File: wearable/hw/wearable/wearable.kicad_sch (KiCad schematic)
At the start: 39 parts, among them Q20 ${ALTIUM_VALUE}, Q21 ${ALTIUM_VALUE}, U2 ${ALTIUM_VALUE}, X20 ${ALTIUM_VALUE}

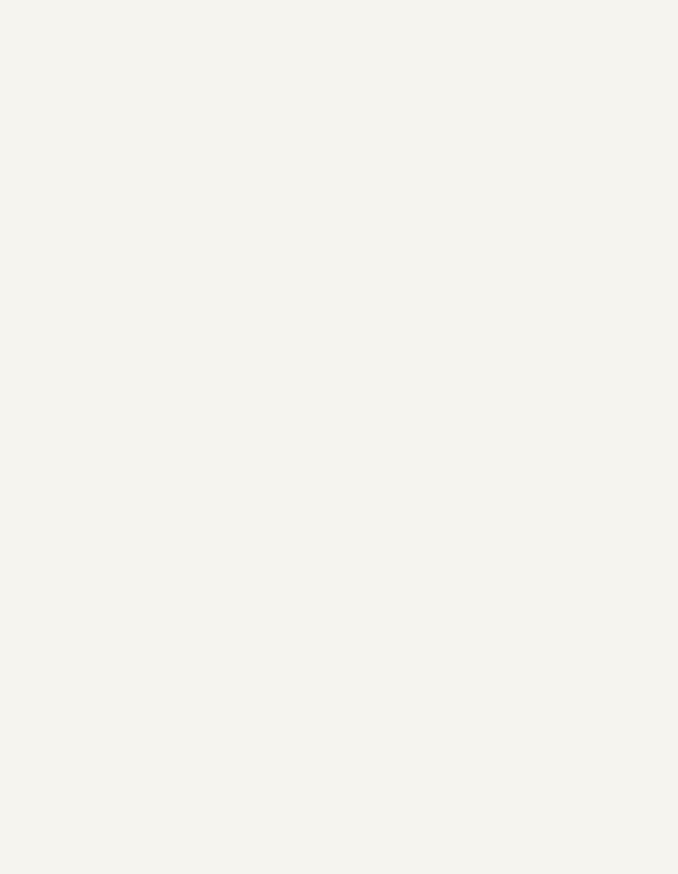
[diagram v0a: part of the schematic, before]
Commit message: Added symbols and stuff to library
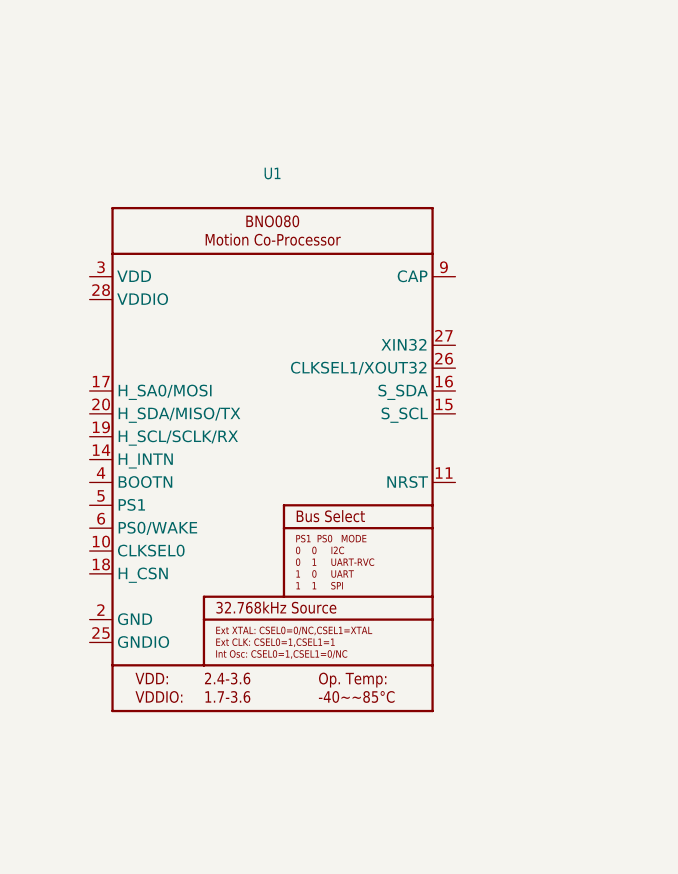
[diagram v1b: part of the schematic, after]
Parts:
- added U1: ~, Adafruit_BNO08x:BNO080, symbol BNO085:BNO080

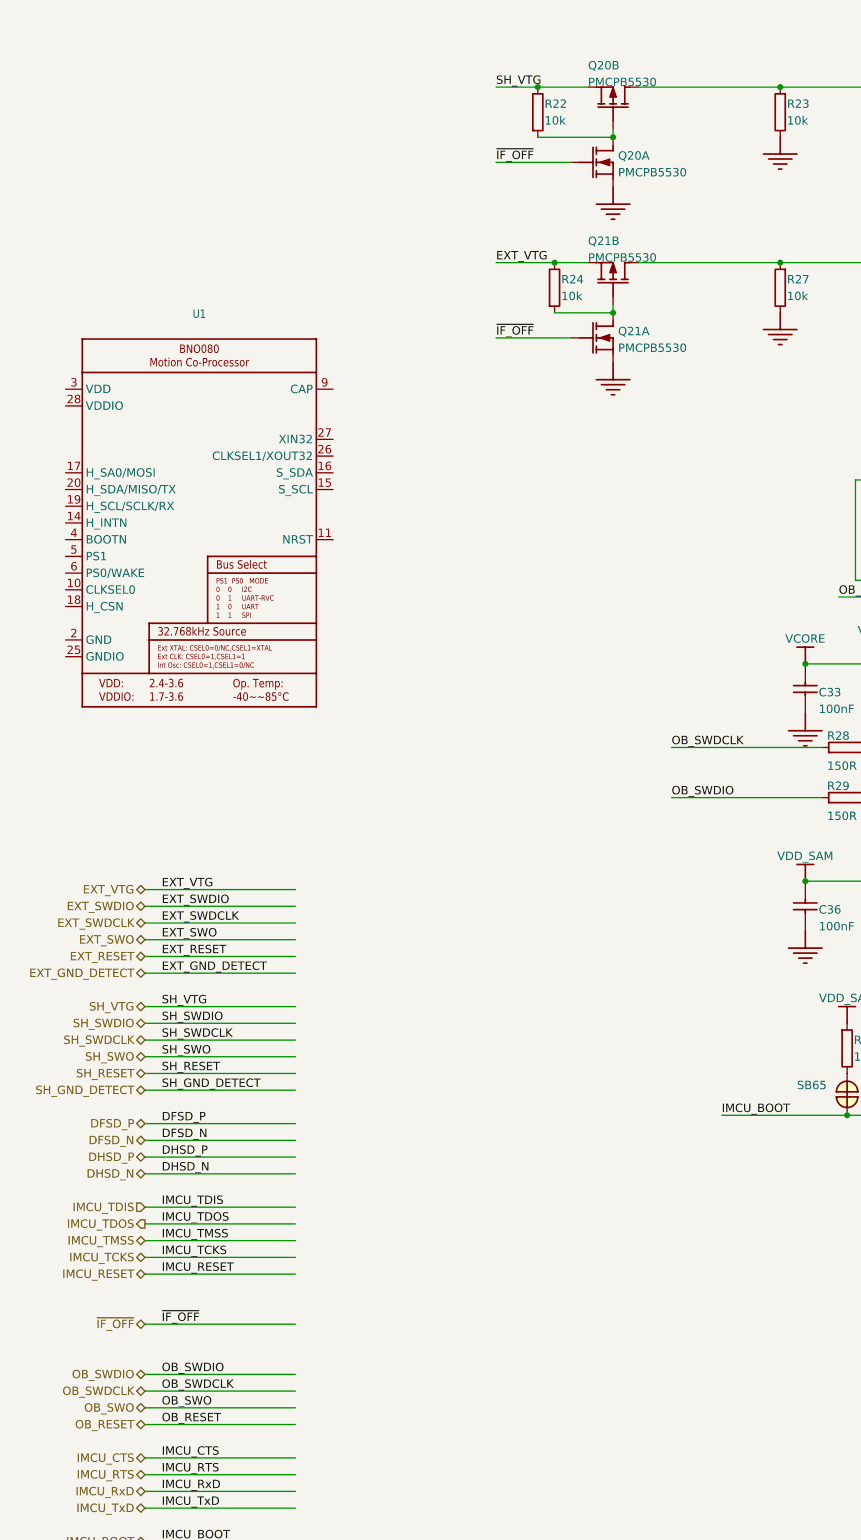
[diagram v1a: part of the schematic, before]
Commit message: Updated schematic with needed parts
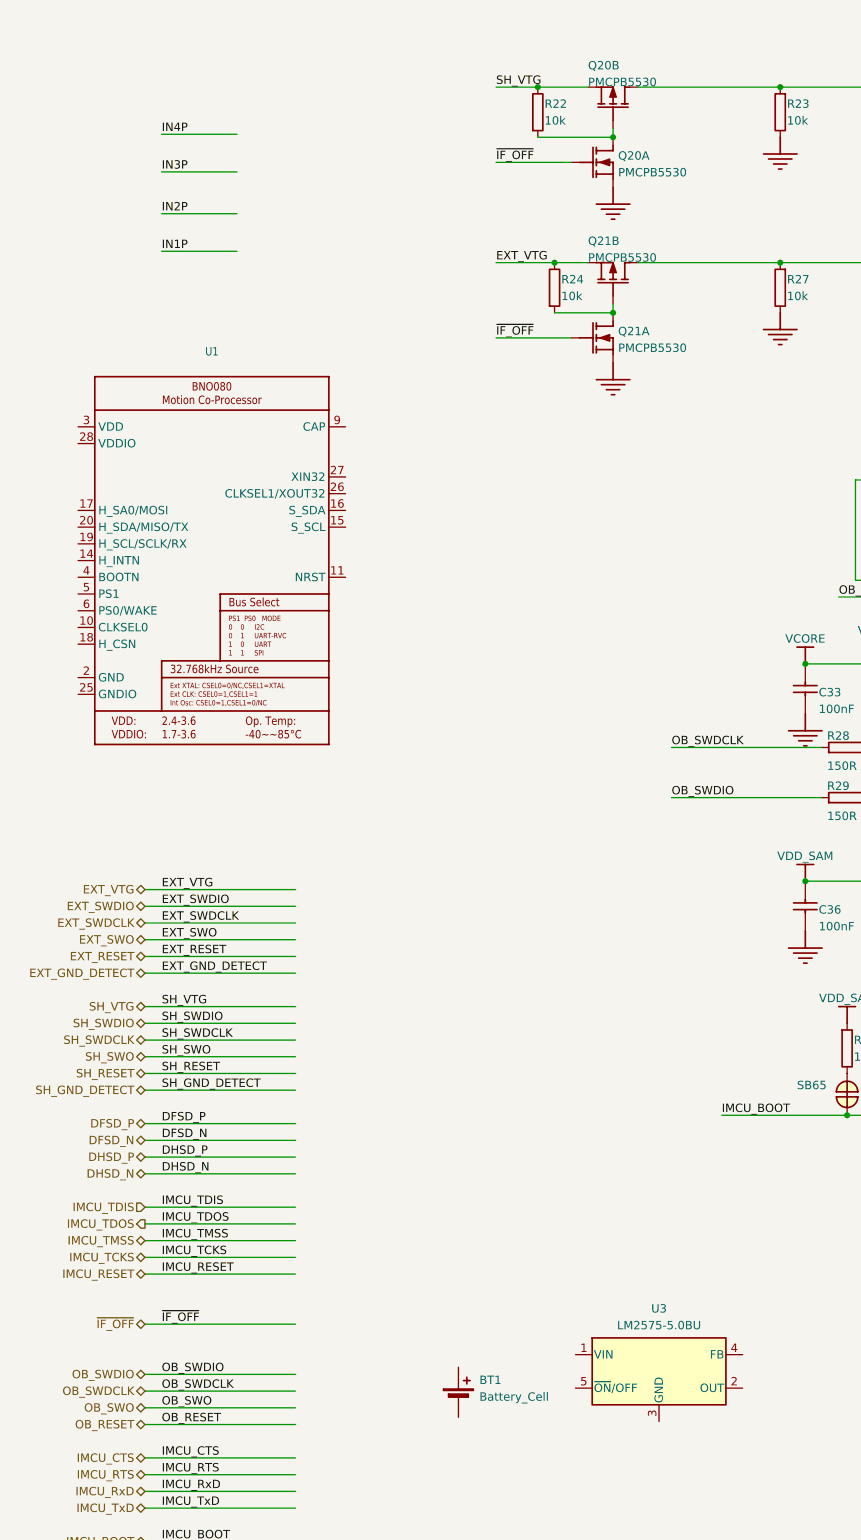
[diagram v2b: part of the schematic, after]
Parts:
- added BT1: Battery_Cell, symbol Device:Battery_Cell
- added U3: LM2575-5.0BU, Package_TO_SOT_SMD:TO-263-5_TabPin3, symbol Regulator_Switching:LM2575-5.0BU
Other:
- moved on the sheet: U1

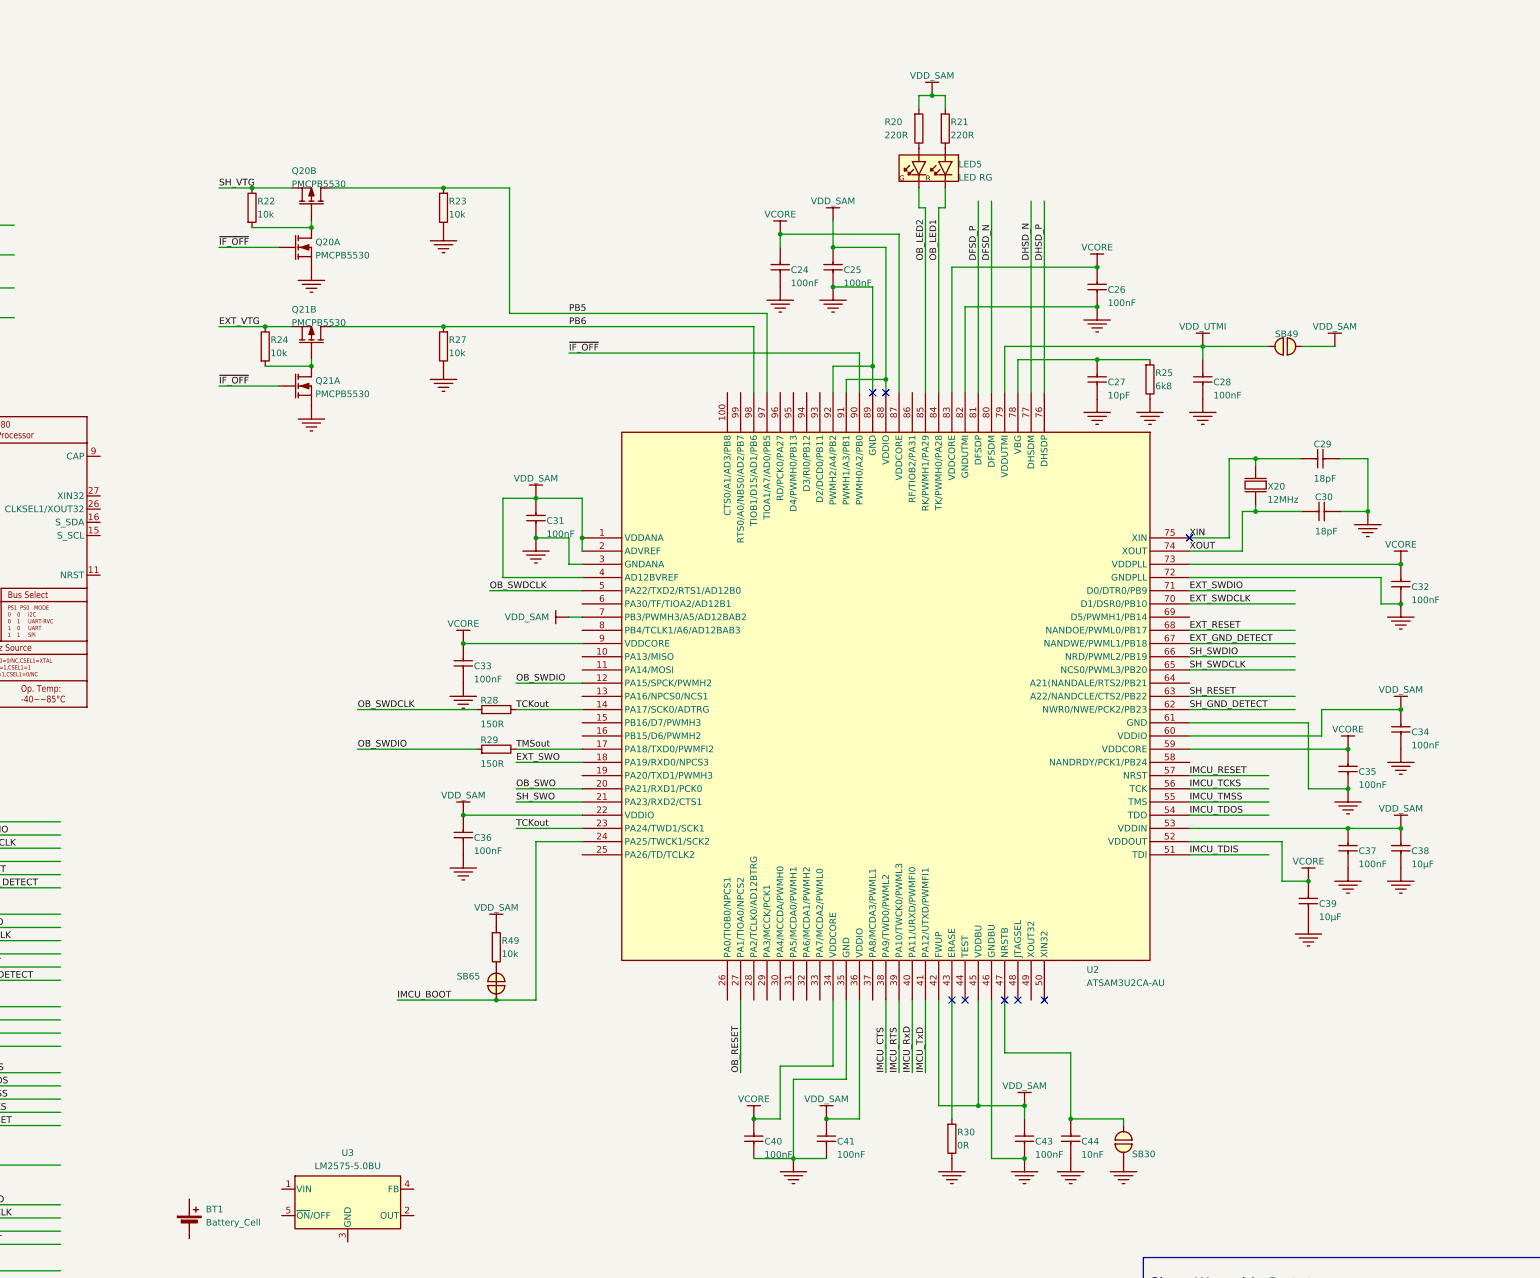
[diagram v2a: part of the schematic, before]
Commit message: Added 445L footprints/symbols and changed some stuff
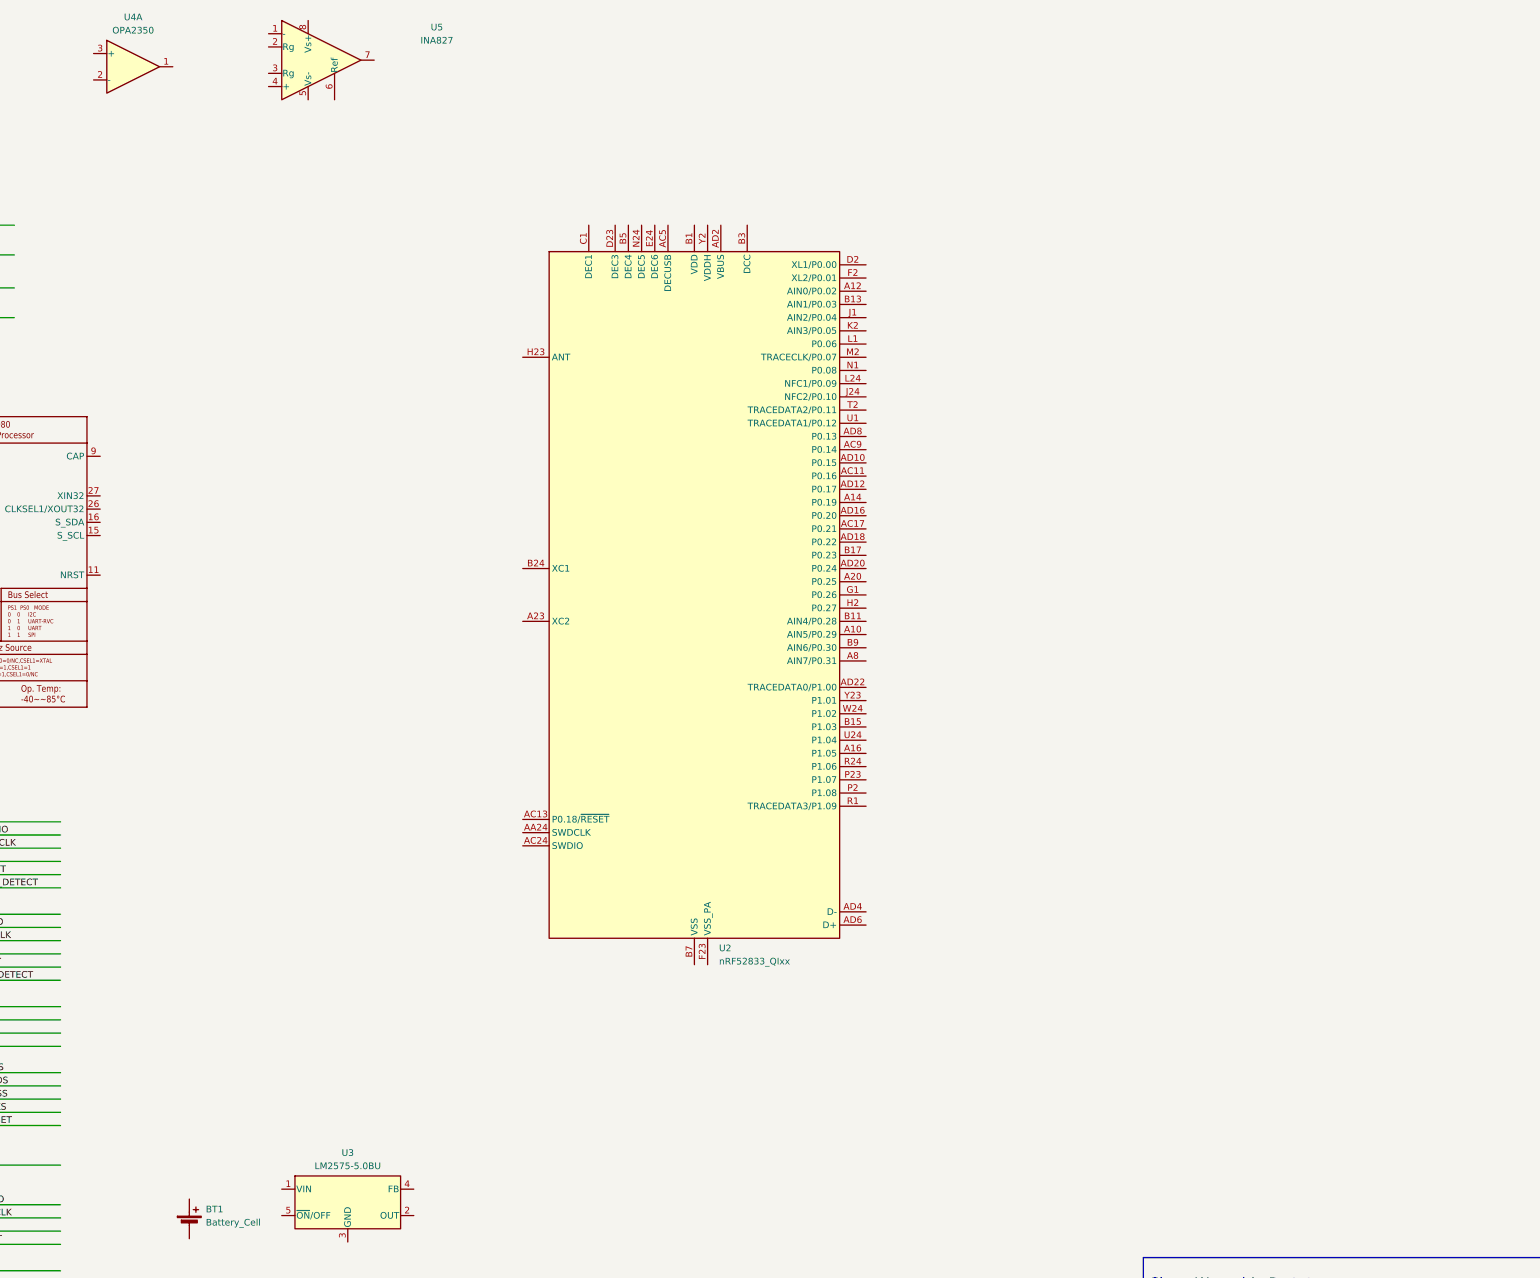
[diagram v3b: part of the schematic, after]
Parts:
- removed C24, C25, C26, C27, C28, C31, C33, C34, C35, C36, C37, C40, C41, C43, C44: ${ALTIUM_VALUE}, CAPC0603X03L_C, symbol wearable-altium-import:root_1_CAP
- removed C29, C30: ${ALTIUM_VALUE}, CAPC0603X03L_C, symbol wearable-altium-import:root_0_CAP
- removed C32: ${ALTIUM_VALUE}, CAPC0603X03L_C, symbol wearable-altium-import:root_3_CAP
- removed C38, C39: ${ALTIUM_VALUE}, CAPC1608X06L, symbol wearable-altium-import:root_1_CAP
- removed LED5: ${ALTIUM_VALUE}, LED_DUAL_0606, symbol wearable-altium-import:root_0_mirrored_D{colon}LED_DUAL_RG
- removed Q20: ${ALTIUM_VALUE}, PMCPB5530X, symbol wearable-altium-import:root_1_T{colon}FET-N/P-DUAL
- removed Q21: ${ALTIUM_VALUE}, PMCPB5530X, symbol wearable-altium-import:root_0_T{colon}FET-N/P-DUAL
- removed R20, R21, R25, R30, R49: ${ALTIUM_VALUE}, RESC0603X03L_C, symbol wearable-altium-import:root_1_RES
- removed R22, R24: ${ALTIUM_VALUE}, RESC0603X03L_C, symbol wearable-altium-import:root_3_mirrored_RES
- removed R23, R27: ${ALTIUM_VALUE}, RESC0603X03L_C, symbol wearable-altium-import:root_1_mirrored_RES
- removed R28, R29: ${ALTIUM_VALUE}, RESC0603X03L_C, symbol wearable-altium-import:root_2_RES
- removed SB30: ${ALTIUM_VALUE}, Solderbridge, symbol wearable-altium-import:root_1_SOLDERBRIDGE
- removed SB49: ${ALTIUM_VALUE}, Solderbridge, symbol wearable-altium-import:root_0_SOLDERBRIDGE
- removed SB65: ${ALTIUM_VALUE}, Solderbridge_Shorted, symbol wearable-altium-import:root_3_SOLDERBRIDGE_SHORTED
- removed U2: ${ALTIUM_VALUE}, TSQFP50P1600X1600X160-100N, symbol wearable-altium-import:root_0_ATSAM3UxCA-AU
- removed X20: ${ALTIUM_VALUE}, BT-XTAL_3225, symbol wearable-altium-import:root_1_XTAL_4-pin_grounded
- added U2: nRF52833_QIxx, Package_DFN_QFN:Nordic_AQFN-73-1EP_7x7mm_P0.5mm, symbol MCU_Nordic:nRF52833_QIxx
- added U4: OPA2350, ECE445L:DIP-8_W7.62mm_LongPads, symbol ECE 445L_old:OPA2350
- added U5: INA827, ECE445L:VSSOP-8_3.0x3.0mm_P0.65mm, symbol ECE 445L_old:INA827
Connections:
- new net: U2.A22 (VDD), U2.AD14 (VDD), U2.AD23 (VDD), U2.B1 (VDD), U2.W1 (VDD)
- new net: U2.B7 (VSS), U2.EP (VSS)
- no-connect marks 8 -> 0

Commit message: hw
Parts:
- removed U4: OPA2350, ECE445L:DIP-8_W7.62mm_LongPads, symbol ECE 445L_old:OPA2350
- removed U5: INA827, ECE445L:VSSOP-8_3.0x3.0mm_P0.65mm, symbol ECE 445L_old:INA827
- added C1, C2: 2uF, symbol Device:C
- added C3, C5: 0.1uF, symbol Device:C
- added C4: 3.3uF, symbol Device:C
- added C6, C7, C8: 0.015uF, symbol Device:C
- added D1: MBR360, DIOAD2860W130L840D505, symbol MBR360:MBR360
- added IC1: AD627ANZ, DIP794W56P254L959H533Q8N, symbol AD627ANZ:AD627ANZ
- added IC2: LM4041CILPR, ECE445L:ti_LM4041CILPR, symbol ti_LM4041CILPR:LM4041CILPR
- added IC3: LM2937ET-3.3_NOPB, ECE445L:TO254P470X1028X1955-3P, symbol ECE445L:LM2937ET-3.3_NOPB
- added L1: 330uF, symbol Device:L
- added R1, R2: R_US, symbol Device:R_US
- added R10: 5.1k, symbol Device:R_US
- added R3: 39k, symbol Device:R_US
- added R4, R5: 1M, symbol Device:R_US
- added R6: 1k, symbol Device:R_US
- added R7: 200k, symbol Device:R_US
- added R8, R9: 49k, symbol Device:R_US
- added U4: OP1177AR, Package_SO:SOIC-8_3.9x4.9mm_P1.27mm, symbol Amplifier_Operational:OP1177AR
- added U5: OP249, Package_CSP:LFCSP-8_2x2mm_P0.5mm, symbol Amplifier_Operational:OP249
- added power_C1: 100uF, symbol Device:C_Polarized
- added power_C2: 220uF, symbol Device:C_Polarized
- added power_C3, power_C4: 4.7uF, ECE445L:CP_Radial_Tantal200mil, symbol ECE445L:C_Polarized
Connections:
- net at U3.1 (VIN): now also BT1.1 (+), power_C1.1
- net at U3.2 (OUT): now also D1.1 (K), L1.1
- net GND: now reaches U3.3 (GND)
- net GND: now also BT1.2 (-), U3.5 (~{ON}/OFF), C3.2, C5.2, D1.2 (A), IC1.4 (-VS), IC2.1, IC2.3, IC3.2 (GND), U4.4 (V-), power_C1.2, power_C2.2, power_C3.2, power_C4.2
- net 5V: now reaches U3.4 (FB)
- net 5V: now also IC3.1 (INPUT), L1.2, power_C2.1, power_C3.1
- new net: C6.2, C7.2, C8.2, IC1.5 (REF), IC2.2, R1.2, R10.1, R2.1, R4.2, R6.1, R8.2, R9.1
- new net: C4.1, IC1.6 (OUTPUT)
- new net: C4.2, R4.1, U4.3 (+)
- new net: R5.1, R6.2, R7.1
- new net: R7.2, R8.1, U4.6
- new net: C2.2, IC1.3 (+IN), R2.2
- new net: R5.2, U4.2 (-)
- new net: C6.1, R9.2, U5.3 (+)
- new net: IC1.1 (RG_1), R3.1
- new net: IC1.8 (RG_2), R3.2
- new net: C1.2, IC1.2 (-IN), R1.1
- new net 3.3V: C3.1, C5.1, IC1.7 (+VS), IC3.3 (OUTPUT), R10.2, U4.7 (V+), power_C4.1
- new net EL1: C1.1
- new net EL2: C2.1
- new net data: C7.1, C8.1, U5.1, U5.2 (-)
- no-connect marks 0 -> 80
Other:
- moved on the sheet: BT1, U1, U2, U3
